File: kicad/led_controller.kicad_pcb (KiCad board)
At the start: 2 copper layers, 60 x 40 mm, 64 parts, among them J1 ISCP_HEADER, J10 CONN_01X01, J11 12V, J12 RED, J13 GREEN, J14 BLUE, J15 CONN_01X01, J16 CONN_01X01, J17 CONN_01X01, J18 CONN_01X01, J2 CONN_01X03, J3 CONN_01X03, J4 CONN_01X03, J5 OLED, J6 CONN_01X01, J7 CONN_01X01, J8 CONN_01X02, J9 CONN_01X01, Q1 IRF8721PBF-1, Q2 IRF8721PBF-1, Q3 IRF8721PBF-1, SW1 Rotary_Encoder_Switch, SW2 Rotary_Encoder_Switch, SW3 Rotary_Encoder_Switch, SW4 Rotary_Encoder_Switch, U1 AP1117-33, U2 ATMEGA328P-AU, U3 INA219, Y1 16Mhz

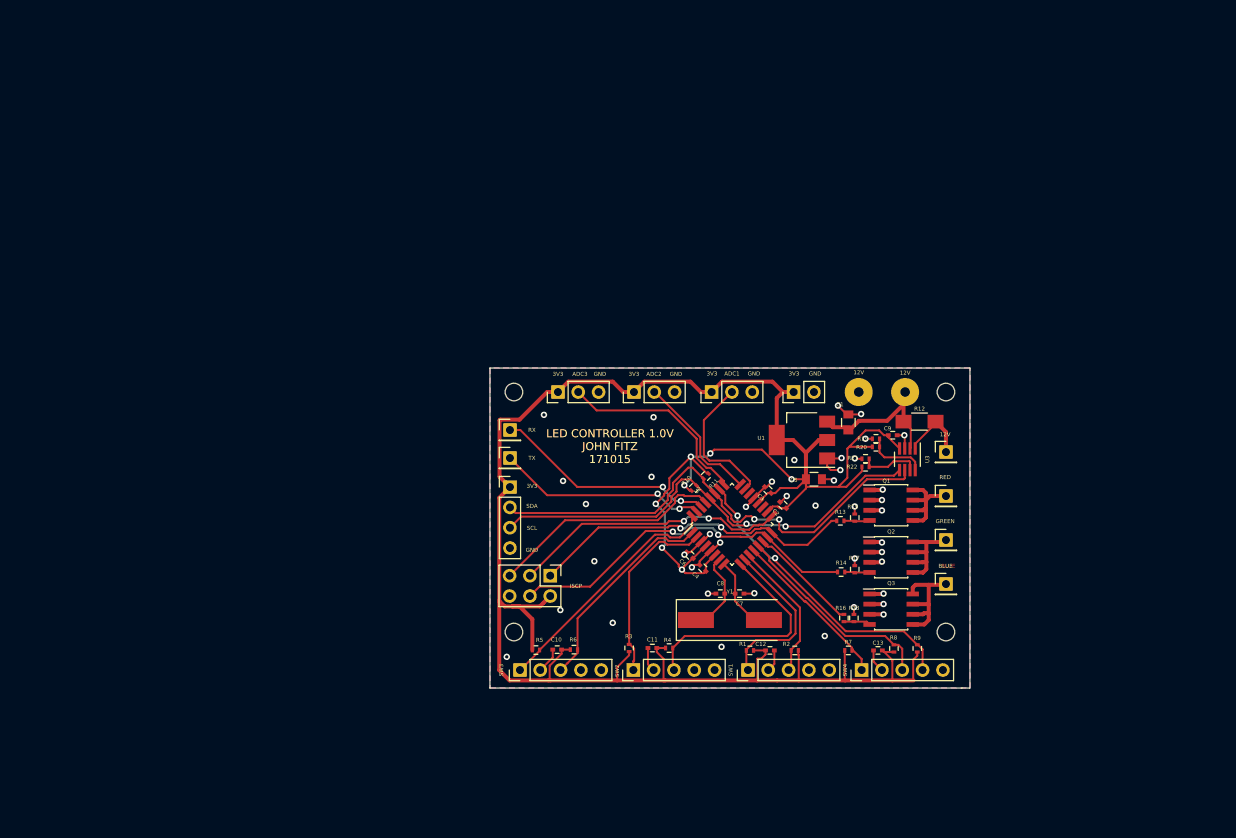
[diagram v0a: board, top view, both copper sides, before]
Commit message: switches to kicad and updates schematic and footprints
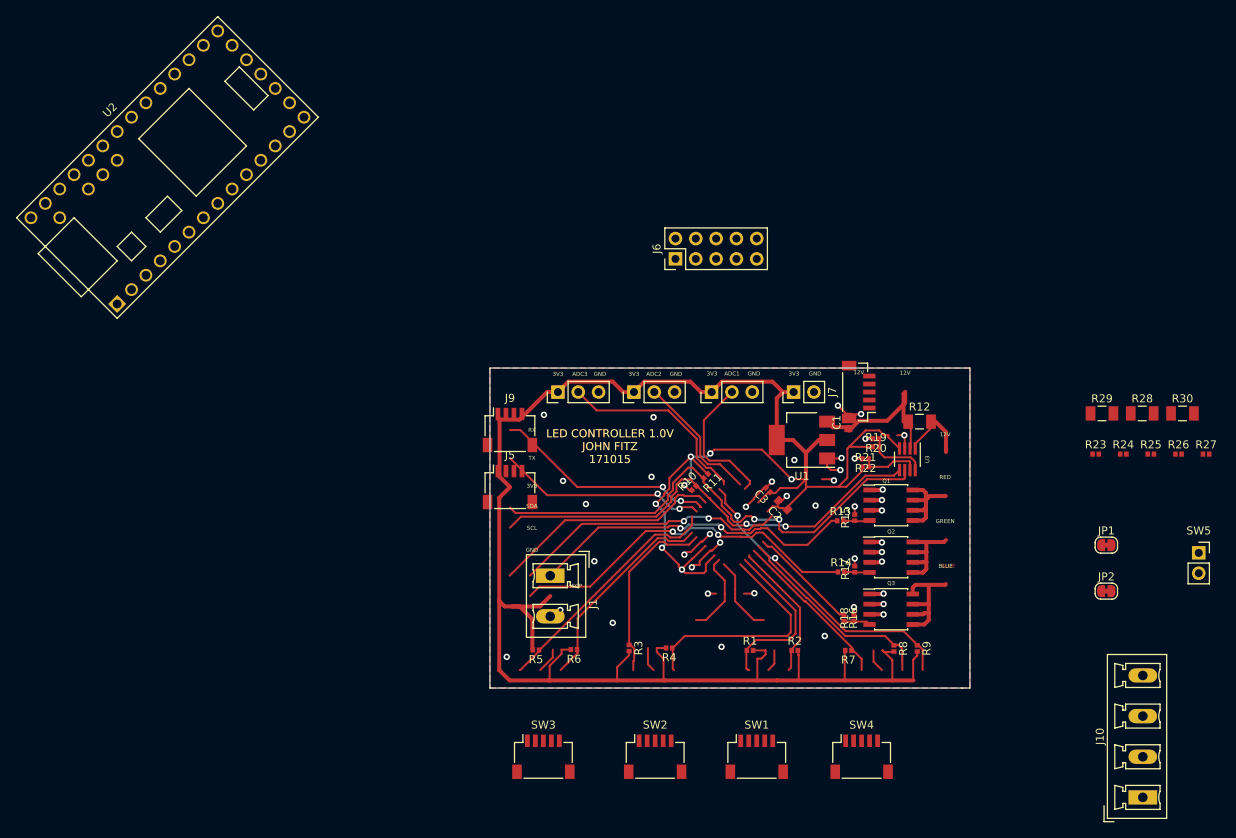
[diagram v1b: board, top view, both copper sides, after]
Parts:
- removed C10, C11, C12, C13, C4, C6, C9: 0.1uF, Capacitors_SMD:C_0402
- removed C5: 10uF, Capacitors_SMD:C_0805
- removed C7, C8: 22pF, Capacitors_SMD:C_0402
- removed J11: 12V, Pin_Headers:Pin_Header_Straight_1x01_Pitch2.54mm
- removed J12: RED, Pin_Headers:Pin_Header_Straight_1x01_Pitch2.54mm
- removed J13: GREEN, Pin_Headers:Pin_Header_Straight_1x01_Pitch2.54mm
- removed J14: BLUE, Pin_Headers:Pin_Header_Straight_1x01_Pitch2.54mm
- removed J15, J16, J17, J18: CONN_01X01, Mounting_Holes:MountingHole_2.2mm_M2
- removed Y1: 16Mhz, Crystals:Crystal_SMD_HC49-SD
- added JP1: Jumper_NC_Small, Jumper:SolderJumper-2_P1.3mm_Bridged_RoundedPad1.0x1.5mm, F.Cu at (177.1, 122.1)
- added JP2: Jumper_NC_Small, Jumper:SolderJumper-2_P1.3mm_Bridged_RoundedPad1.0x1.5mm, F.Cu at (177.1, 127.9)
- added R23: 10K, Resistor_SMD:R_0402_1005Metric, F.Cu at (175.7, 110.8)
- added R24: 10K, Resistor_SMD:R_0402_1005Metric, F.Cu at (179.2, 110.8)
- added R25: 10K, Resistor_SMD:R_0402_1005Metric, F.Cu at (182.6, 110.8)
- added R26: 10K, Resistor_SMD:R_0402_1005Metric, F.Cu at (186.1, 110.8)
- added R27: 10K, Resistor_SMD:R_0402_1005Metric, F.Cu at (189.5, 110.8)
- added R28: 0R1, Resistor_SMD:R_1206_3216Metric, F.Cu at (181.5, 105.7)
- added R29: 0R1, Resistor_SMD:R_1206_3216Metric, F.Cu at (176.5, 105.7)
- added R30: 0R1, Resistor_SMD:R_1206_3216Metric, F.Cu at (186.6, 105.7)
- added SW5: SW_DIP_x01, Connector_PinSocket_2.54mm:PinSocket_1x02_P2.54mm_Vertical, F.Cu at (188.6, 123.1)
- C1: value 0.1uF -> 10uF; footprint Capacitors_SMD:C_0805 -> Capacitor_SMD:C_0603_1608Metric
- C2: value 0.1uF -> 10uF; footprint Capacitors_SMD:C_0402 -> Capacitor_SMD:C_0603_1608Metric
- C3: footprint Capacitors_SMD:C_0402 -> Capacitor_SMD:C_0402_1005Metric
- J1: value ISCP_HEADER -> PWR_IN; footprint Pin_Headers:Pin_Header_Straight_2x03_Pitch2.54mm -> Connector_Phoenix_MC:PhoenixContact_MCV_1,5_2-G-5.08_1x02_P5.08mm_Vertical
- J10: value CONN_01X01 -> Conn_01x04; footprint Pin_Headers:Pin_Header_Straight_1x01_Pitch2.54mm -> Connector_Phoenix_MC:PhoenixContact_MCV_1,5_4-G-5.08_1x04_P5.08mm_Vertical
- J2: value CONN_01X03 -> ADC1
- J3: value CONN_01X03 -> ADC2
- J4: value CONN_01X03 -> ADC3
- J5: value OLED -> I2C; footprint Pin_Headers:Pin_Header_Straight_1x04_Pitch2.54mm -> Connector_JST:JST_SH_SM04B-SRSS-TB_1x04-1MP_P1.00mm_Horizontal
- J6: value CONN_01X01 -> UEXT; footprint Wire_Pads:SolderWirePad_single_1-2mmDrill -> Connector_PinHeader_2.54mm:PinHeader_2x05_P2.54mm_Vertical
- J7: value CONN_01X01 -> SPI; footprint Wire_Pads:SolderWirePad_single_1-2mmDrill -> Connector_JST:JST_SH_BM05B-SRSS-TB_1x05-1MP_P1.00mm_Vertical
- J8: value CONN_01X02 -> 5V
- J9: value CONN_01X01 -> UART; footprint Pin_Headers:Pin_Header_Straight_1x01_Pitch2.54mm -> Connector_JST:JST_SH_SM04B-SRSS-TB_1x04-1MP_P1.00mm_Horizontal
- R1, R10, R11, R13, R14, R15, R16, R17, R18, R19, R2, R20, R21, R22, R3, R4, R5, R6, R7, R8, R9: footprint Resistors_SMD:R_0402 -> Resistor_SMD:R_0402_1005Metric
- R12: footprint Resistors_SMD:R_1206_HandSoldering -> Resistor_SMD:R_1206_3216Metric
- SW1, SW2, SW3, SW4: footprint Pin_Headers:Pin_Header_Straight_1x05_Pitch2.54mm -> Connector_JST:JST_SH_SM05B-SRSS-TB_1x05-1MP_P1.00mm_Horizontal
- U1: value AP1117-33 -> AP1117-ADJ; footprint TO_SOT_Packages_SMD:SOT-223-3Lead_TabPin2 -> Package_TO_SOT_SMD:SOT-223-3_TabPin2
- U2: value ATMEGA328P-AU -> Teensy-LC; footprint Housings_QFP:TQFP-32_7x7mm_Pitch0.8mm -> teensy:Teensy30_31_32_LC
- moved J10 89.8 mm to (181.6, 153.7), turned to 90 degrees
- moved U2 83.5 mm to (59.7, 74.9)
- moved J6 33.2 mm to (123.2, 86.4)
- moved SW3 11.2 mm to (106.7, 148.6), turned to 0 degrees
- moved SW2 11.2 mm to (120.7, 148.6), turned to 0 degrees
- moved SW1 10.9 mm to (133.3, 148.6), turned to 0 degrees
- moved SW4 10.8 mm to (146.5, 148.6), turned to 0 degrees
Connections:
- C2 pad 1: +3V3 -> +5V
- J1 pad 1: /PWM_B -> GND
- J1 pad 2: +3V3 -> +12V
- J10 pad 1: /TX -> Net-(J10-Pad1)
- J5 pad 2: /I2C_SDA -> /SDA
- J5 pad 3: /I2C_SCL -> /SCL
- J6 pad 1: +12V -> Net-(J6-Pad1)
- J7 pad 1: GND -> +3V3
- J8 pad 1: +3V3 -> +5V
- J9 pad 1: /RX -> +3V3
- Q1 pad 5: Net-(J12-Pad1) -> Net-(J10-Pad3)
- Q1 pad 6: Net-(J12-Pad1) -> Net-(J10-Pad3)
- Q1 pad 7: Net-(J12-Pad1) -> Net-(J10-Pad3)
- Q1 pad 8: Net-(J12-Pad1) -> Net-(J10-Pad3)
- Q2 pad 5: Net-(J13-Pad1) -> Net-(J10-Pad2)
- Q2 pad 6: Net-(J13-Pad1) -> Net-(J10-Pad2)
- Q2 pad 7: Net-(J13-Pad1) -> Net-(J10-Pad2)
- Q2 pad 8: Net-(J13-Pad1) -> Net-(J10-Pad2)
- Q3 pad 5: Net-(J14-Pad1) -> Net-(J10-Pad1)
- Q3 pad 6: Net-(J14-Pad1) -> Net-(J10-Pad1)
- Q3 pad 7: Net-(J14-Pad1) -> Net-(J10-Pad1)
- Q3 pad 8: Net-(J14-Pad1) -> Net-(J10-Pad1)
- R1 pad 1: /ENC_3A -> /ENC_1A
- R10 pad 2: /I2C_SCL -> Net-(JP2-Pad1)
- R11 pad 2: /I2C_SDA -> Net-(JP1-Pad1)
- R12 pad 2: Net-(J11-Pad1) -> Net-(J10-Pad4)
- R2 pad 1: /ENC_3B -> /ENC_1B
- R5 pad 1: /ENC_1A -> /ENC_3A
- R6 pad 1: /ENC_1B -> /ENC_3B
- R9 pad 1: Net-(R9-Pad1) -> /SW4
- SW1 pad 1: /ENC_3A -> (no net)
- SW1 pad 2: GND -> (no net)
- SW1 pad 3: /ENC_3B -> (no net)
- SW1 pad 4: Net-(SW1-Pad4) -> (no net)
- SW1 pad 5: Net-(SW1-Pad5) -> (no net)
- SW2 pad 1: /ENC_2A -> (no net)
- SW2 pad 2: GND -> (no net)
- SW2 pad 3: /ENC_2B -> (no net)
- SW2 pad 4: Net-(SW2-Pad4) -> (no net)
- SW2 pad 5: Net-(SW2-Pad5) -> (no net)
- SW3 pad 1: /ENC_1A -> (no net)
- SW3 pad 2: GND -> (no net)
- SW3 pad 3: /ENC_1B -> (no net)
- SW3 pad 4: Net-(SW3-Pad4) -> (no net)
- SW3 pad 5: Net-(SW3-Pad5) -> (no net)
- SW4 pad 1: /ENC_4A -> (no net)
- SW4 pad 2: GND -> (no net)
- SW4 pad 3: /ENC_4B -> (no net)
- SW4 pad 4: Net-(R9-Pad1) -> (no net)
- SW4 pad 5: GND -> (no net)
- U1 pad 1: GND -> Net-(R23-Pad2)
- U1 pad 2: +3V3 -> Net-(R23-Pad1)
- U2 pad 1: /ENC_1B -> Net-(U2-Pad1)
- U2 pad 10: /ENC_3A -> /ENC_4B
- U2 pad 11: /ENC_3B -> /SW1
- U2 pad 12: /ENC_4A -> /CS0
- U2 pad 13: /ENC_4B -> /MOSI0
- U2 pad 14: /PWM_R -> /MISO0
- U2 pad 15: /PWM_G -> Net-(U2-Pad15)
- U2 pad 16: /PWM_B -> Net-(U2-Pad16)
- U2 pad 17: Net-(J1-Pad3) -> GND
- U2 pad 18: +3V3 -> Net-(U2-Pad18)
- U2 pad 19: Net-(U2-Pad19) -> /SW2
- U2 pad 2: /ENC_2A -> /RX
- U2 pad 20: +3V3 -> Net-(U2-Pad20)
- U2 pad 21: GND -> /SCK0
- U2 pad 22: Net-(U2-Pad22) -> /ADC_1
- U2 pad 23: /ADC_1 -> /ADC_2
- U2 pad 24: /ADC_2 -> /ADC_3
- U2 pad 25: /ADC_3 -> /SDA
- U2 pad 26: Net-(R9-Pad1) -> /SCL
- U2 pad 27: /I2C_SDA -> /PWM_R
- U2 pad 28: /I2C_SCL -> /SW3
- U2 pad 29: Net-(J1-Pad5) -> /PWM_G
- U2 pad 3: GND -> /TX
- U2 pad 30: /RX -> /PWM_B
- U2 pad 31: /TX -> +3V3
- U2 pad 32: /ENC_1A -> GND
- U2 pad 4: +3V3 -> /ENC_1A
- U2 pad 5: GND -> /ENC_1B
- U2 pad 6: +3V3 -> /ENC_2A
- U2 pad 7: Net-(C8-Pad2) -> /ENC_3A
- U2 pad 8: Net-(C7-Pad2) -> /ENC_3B
- U2 pad 9: /ENC_2B -> /ENC_4A
- U3 pad 1: Net-(J11-Pad1) -> Net-(J10-Pad4)
- U3 pad 5: /I2C_SCL -> Net-(JP2-Pad1)
- U3 pad 6: /I2C_SDA -> Net-(JP1-Pad1)
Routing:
- net Net-(JP1-Pad1): track 0.00 -> 62.2 mm, vias 0 -> 2
- net /I2C_SDA: track 62.2 -> 0.00 mm, vias 2 -> 0
- net Net-(JP2-Pad1): track 0.00 -> 57.9 mm, vias 0 -> 2
- net /I2C_SCL: track 57.9 -> 0.00 mm, vias 2 -> 0
- net Net-(R9-Pad1): track 37.8 -> 0.00 mm, vias 2 -> 0
- net /SW4: track 0.00 -> 37.8 mm, vias 0 -> 2
- net Net-(U2-Pad37): track 0.00 -> 34.7 mm, vias 0 -> 2
- net Net-(J1-Pad3): track 34.7 -> 0.00 mm, vias 2 -> 0
- net GND: track 60.8 -> 43.0 mm, vias 42 -> 38
- net Net-(J14-Pad1): track 15.8 -> 0.00 mm
- net Net-(J10-Pad1): track 0.00 -> 15.8 mm
- net Net-(J13-Pad1): track 12.9 -> 0.00 mm
- net Net-(J10-Pad2): track 0.00 -> 12.9 mm
- net Net-(J12-Pad1): track 12.7 -> 0.00 mm
- net Net-(J10-Pad3): track 0.00 -> 12.7 mm
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
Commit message: finishes placement and power routing
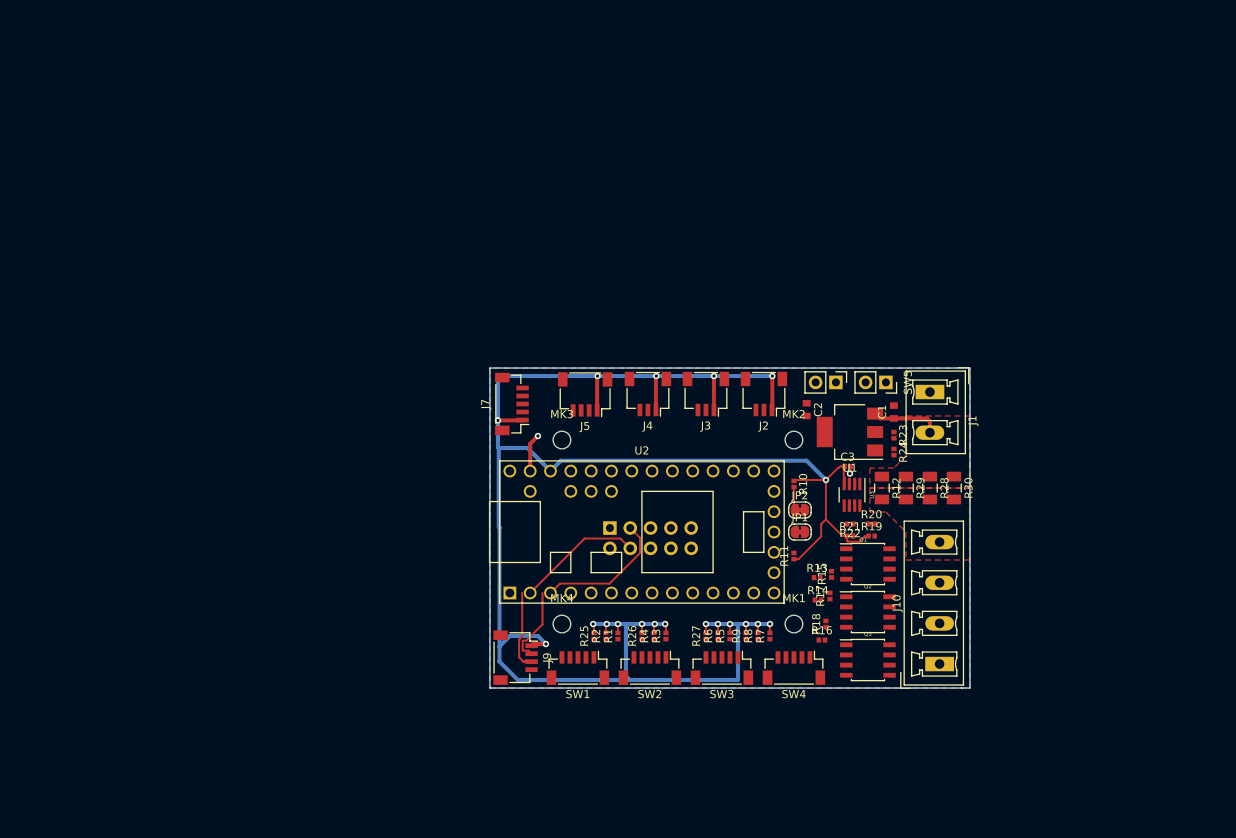
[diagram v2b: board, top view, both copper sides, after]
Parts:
- added MK1: Mounting_Hole, MountingHole:MountingHole_2.2mm_M2, F.Cu at (138.0, 132.0)
- added MK2: Mounting_Hole, MountingHole:MountingHole_2.2mm_M2, F.Cu at (138.0, 109.0)
- added MK3: Mounting_Hole, MountingHole:MountingHole_2.2mm_M2, F.Cu at (109.0, 109.0)
- added MK4: Mounting_Hole, MountingHole:MountingHole_2.2mm_M2, F.Cu at (109.0, 132.0)
- J2, J3, J4: footprint Pin_Headers:Pin_Header_Straight_1x03_Pitch2.54mm -> Connector_JST:JST_SH_SM03B-SRSS-TB_1x03-1MP_P1.00mm_Horizontal
- J6: moved to B.Cu
- SW1, SW2, SW3, SW4: footprint Connector_JST:JST_SH_SM05B-SRSS-TB_1x05-1MP_P1.00mm_Horizontal -> Connector_JST:JST_SH_BM05B-SRSS-TB_1x05-1MP_P1.00mm_Vertical
- moved U2 74.8 mm to (119.0, 120.5), turned to 0 degrees
- moved R25 73.2 mm to (113.0, 133.5), turned to 90 degrees
- moved R26 70.8 mm to (119.0, 133.5), turned to 90 degrees
- moved R27 66.5 mm to (127.0, 133.5), turned to 90 degrees
- moved J1 52.7 mm to (155.0, 103.0)
- moved SW5 44.5 mm to (149.5, 101.8), turned to 270 degrees
- moved J7 43.4 mm to (102.8, 104.5)
- moved JP2 39.6 mm to (138.8, 117.8)
- moved JP1 38.3 mm to (138.8, 120.5)
- moved J6 34.6 mm to (115.0, 120.0), turned to 270 degrees
- moved J10 30.4 mm to (156.2, 137.0)
- moved R30 30.0 mm to (158.0, 115.0), turned to 270 degrees
- moved R24 28.7 mm to (150.5, 110.5), turned to 270 degrees
- moved J9 28.5 mm to (103.2, 136.2), turned to 270 degrees
- moved R28 28.1 mm to (155.0, 115.0), turned to 270 degrees
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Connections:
- net Net-(J10-Pad4) renamed /12V_SHUNT
- J9 pad 2: /RX -> /TX
- J9 pad 3: /TX -> /RX
- SW1 pad 1: (no net) -> /ENC_1A
- SW1 pad 2: (no net) -> GND
- SW1 pad 3: (no net) -> /ENC_1B
- SW1 pad 4: (no net) -> /SW1
- SW1 pad 5: (no net) -> GND
- SW2 pad 1: (no net) -> /ENC_2A
- SW2 pad 2: (no net) -> GND
- SW2 pad 3: (no net) -> /ENC_2B
- SW2 pad 4: (no net) -> /SW2
- SW2 pad 5: (no net) -> GND
- SW3 pad 1: (no net) -> /ENC_3A
- SW3 pad 2: (no net) -> GND
- SW3 pad 3: (no net) -> /ENC_3B
- SW3 pad 4: (no net) -> /SW3
- SW3 pad 5: (no net) -> GND
- SW4 pad 1: (no net) -> /ENC_4A
- SW4 pad 2: (no net) -> GND
- SW4 pad 3: (no net) -> /ENC_4B
- SW4 pad 4: (no net) -> /SW4
- SW4 pad 5: (no net) -> GND
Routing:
- net Net-(JP1-Pad1): track 62.2 -> 0.00 mm, vias 2 -> 0
- net Net-(JP2-Pad1): track 57.9 -> 2.90 mm, vias 2 -> 0
- net /PWM_G: track 45.1 -> 0.00 mm, vias 2 -> 0
- net /PWM_B: track 41.5 -> 0.00 mm, vias 2 -> 0
- net +3V3: track 291.9 -> 251.0 mm, vias 7 -> 19
- net /SW4: track 37.8 -> 0.00 mm, vias 2 -> 0
- net GND: track 43.0 -> 5.72 mm, vias 38 -> 2
- net Net-(U2-Pad37): track 34.7 -> 0.00 mm, vias 2 -> 0
- net /ENC_3A: track 30.5 -> 0.00 mm
- net /ENC_2B: track 29.5 -> 0.00 mm
- net Net-(J1-Pad5): track 29.4 -> 0.00 mm
- net /ENC_1B: track 27.4 -> 0.00 mm
- net /ENC_3B: track 26.4 -> 0.00 mm
- net /ENC_4B: track 26.2 -> 0.00 mm
- net /ADC_3: track 24.6 -> 0.00 mm
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- added copper zone on F.Cu, net +12V
- added copper zone on F.Cu, net /12V_SHUNT
- removed copper zone on F.Cu, net GND
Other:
- net class Default: clearance 0.2 -> 0.25
- net class PWR added: clearance 0.25, trace_width 0.5, via_dia 0.8, via_drill 0.4
- rule trace_clearance: 0.2 -> 0.25
- board text removed: "12V"
- board text removed: "3V3"
- board text removed: "ADC1"
- board text removed: "ADC2"
- board text removed: "ADC3"
- board text removed: "BLUE"
- board text removed: "GND"
- board text removed: "GREEN"
- board text removed: "ISCP"
- board text removed: "LED CONTROLLER 1.0V JOHN FITZ 171015"
- board text removed: "RED"
- board text removed: "RX"
- board text removed: "SCL"
- board text removed: "SDA"
- board text removed: "TX"

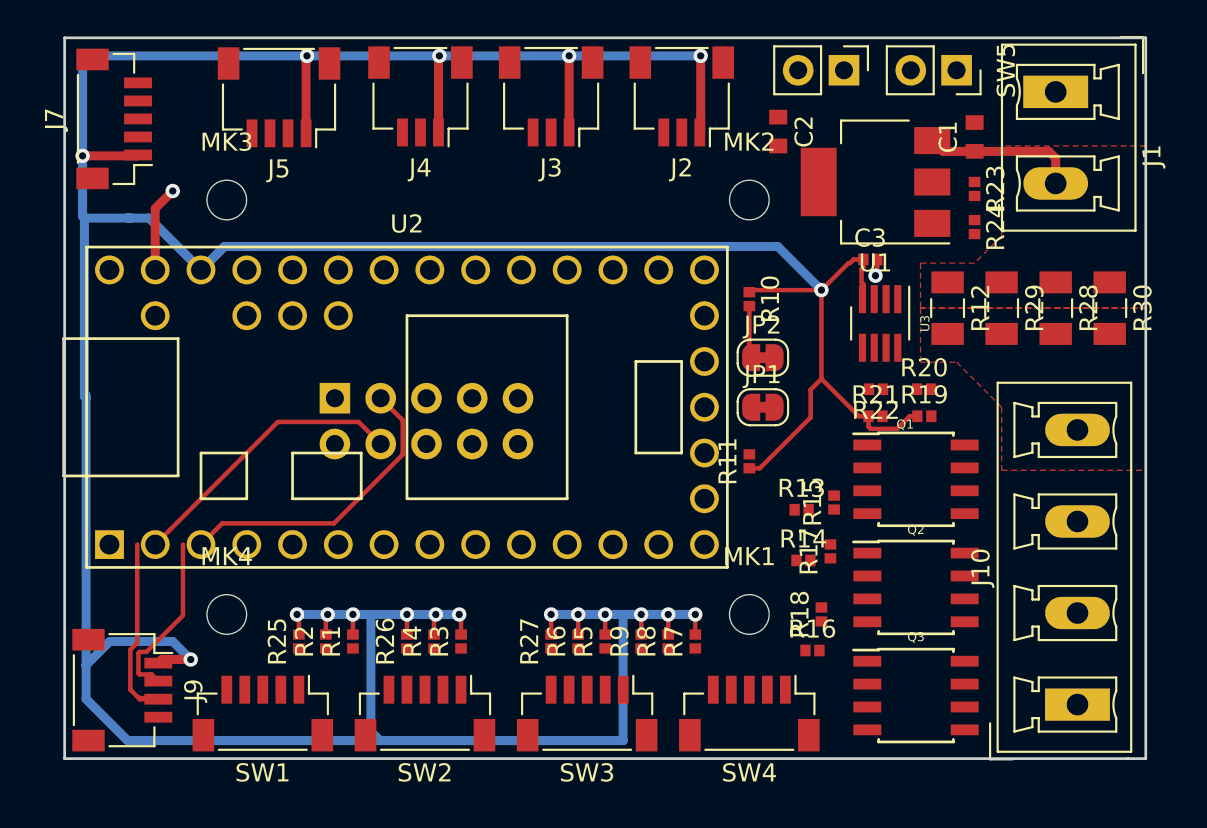
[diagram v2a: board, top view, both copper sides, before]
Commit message: finishes layout, needs look over and silk
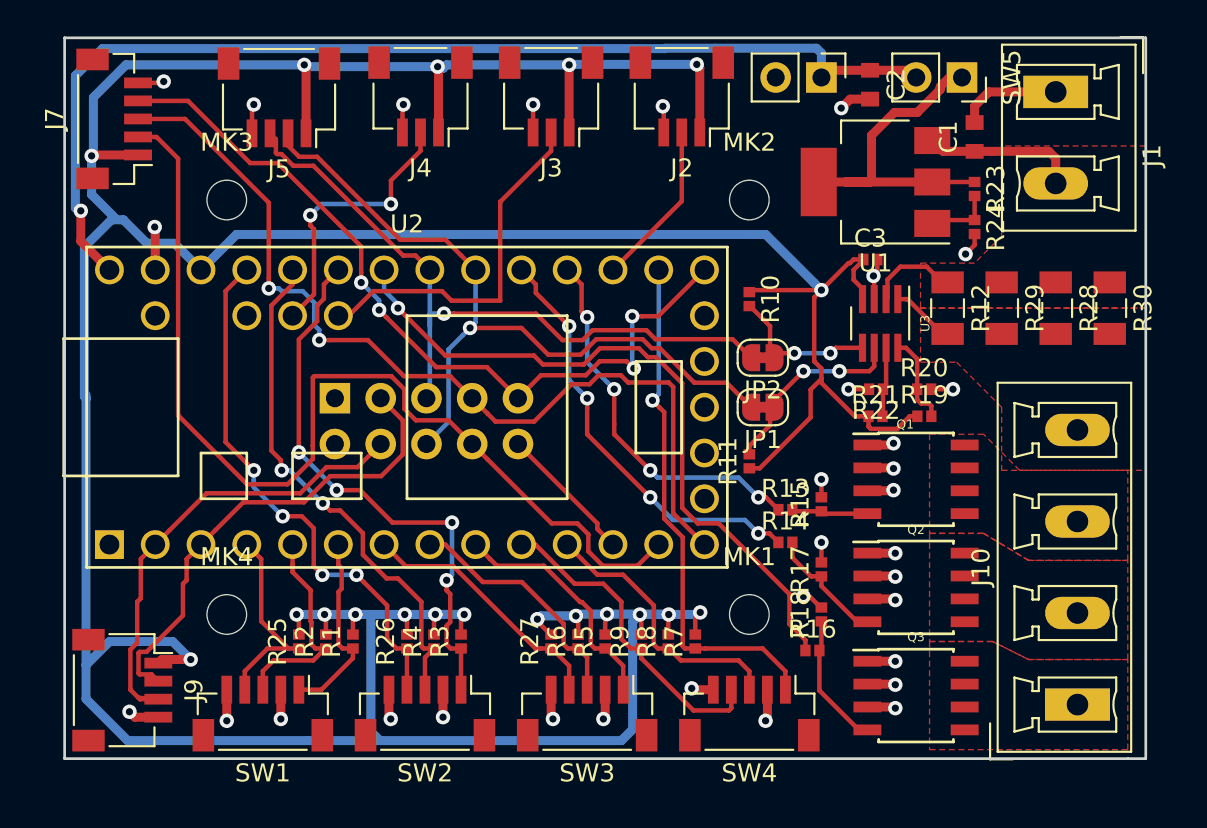
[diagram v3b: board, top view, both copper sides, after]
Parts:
- moved C2 5.72 mm to (144.7, 102.6)
- moved R14 1.41 mm to (140.0, 128.0)
- moved J8 1.31 mm to (142.0, 102.2)
- moved R17 1.12 mm to (142.0, 129.5)
- moved R13 0.90 mm to (140.0, 126.2)
- moved R15 0.71 mm to (142.0, 125.9)
- moved SW5 0.50 mm to (149.8, 102.2)
- turned JP1 to 180 degrees
- turned JP2 to 180 degrees
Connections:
- net Net-(J10-Pad1) renamed /OUT_R
- net Net-(J10-Pad2) renamed /OUT_G
- net Net-(J10-Pad3) renamed /OUT_B
- net Net-(R23-Pad1) renamed /5V_SW
- JP1 pad 2: /I2C_SDA -> /SDA
- JP2 pad 2: /I2C_SCL -> /SCL
- U2 pad 10: /ENC_4B -> /SW4
- U2 pad 11: /SW1 -> /ENC_4B
- U2 pad 19: /SW2 -> Net-(U2-Pad19)
- U2 pad 20: Net-(U2-Pad20) -> /SCK0
- U2 pad 21: /SCK0 -> /ENC_4A
- U2 pad 23: /ADC_2 -> /PWM_B
- U2 pad 24: /ADC_3 -> /PWM_G
- U2 pad 28: /SW3 -> /ENC_2A
- U2 pad 29: /PWM_G -> /ENC_2B
- U2 pad 30: /PWM_B -> /SW2
- U2 pad 36: /SW4 -> /ADC_3
- U2 pad 37: Net-(U2-Pad37) -> /ADC_2
- U2 pad 4: /ENC_1A -> /SW1
- U2 pad 6: /ENC_2A -> /ENC_1A
- U2 pad 7: /ENC_3A -> /SW3
- U2 pad 9: /ENC_4A -> /ENC_3A
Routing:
- net +5V: track 0.00 -> 60.4 mm, vias 0 -> 1
- net /MOSI0: track 0.00 -> 56.4 mm
- net /MISO0: track 0.00 -> 51.3 mm, vias 0 -> 2
- net GND: track 5.72 -> 55.4 mm, vias 2 -> 32
- net /SCK0: track 0.00 -> 44.9 mm, vias 0 -> 4
- net /SDA: track 0.00 -> 42.9 mm, vias 0 -> 1
- net /SCL: track 0.00 -> 39.7 mm, vias 0 -> 1
- net /PWM_R: track 0.00 -> 39.0 mm, vias 0 -> 1
- net /ENC_2A: track 0.00 -> 31.4 mm, vias 0 -> 4
- net /SW2: track 0.00 -> 30.0 mm, vias 0 -> 4
- net /ENC_2B: track 0.00 -> 29.1 mm, vias 0 -> 2
- net /ENC_4A: track 0.00 -> 29.0 mm, vias 0 -> 1
- net /PWM_G: track 0.00 -> 23.7 mm, vias 0 -> 4
- net /PWM_B: track 0.00 -> 21.0 mm, vias 0 -> 4
- net /ADC_2: track 0.00 -> 20.3 mm
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- added copper zone on F.Cu, net /OUT_B
- added copper zone on F.Cu, net /OUT_G
- added copper zone on F.Cu, net /OUT_R
